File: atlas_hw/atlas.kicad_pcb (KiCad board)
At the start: 4 copper layers, 35.4 x 73.4 mm, 121 parts, among them J1 USB_B_Micro, J10 PSP_LCD, J2 DEBUG_STM, J3 PSP_TOUCH, J4 Conn_02x10_Counter_Clockwise, J8 Micro_SD_Card_Det, J9 PSP_LCD_BL, Q4 Q_NMOS_DGS, SW1 SReset, SW2 Power, SW3 ResetSTM, U1 STM32H723VITx, U11 STM6601CA2BDM6F, U12 BGU7007, U13 LSF0108, U14 NPP600SNADJ, U16 PAM2841, U2 W957A8MFYA5I, U3 MCP1811B, U4 TLV62569DBV, U7 Teseo-LIV3F, Y1 16M, Y4 32k

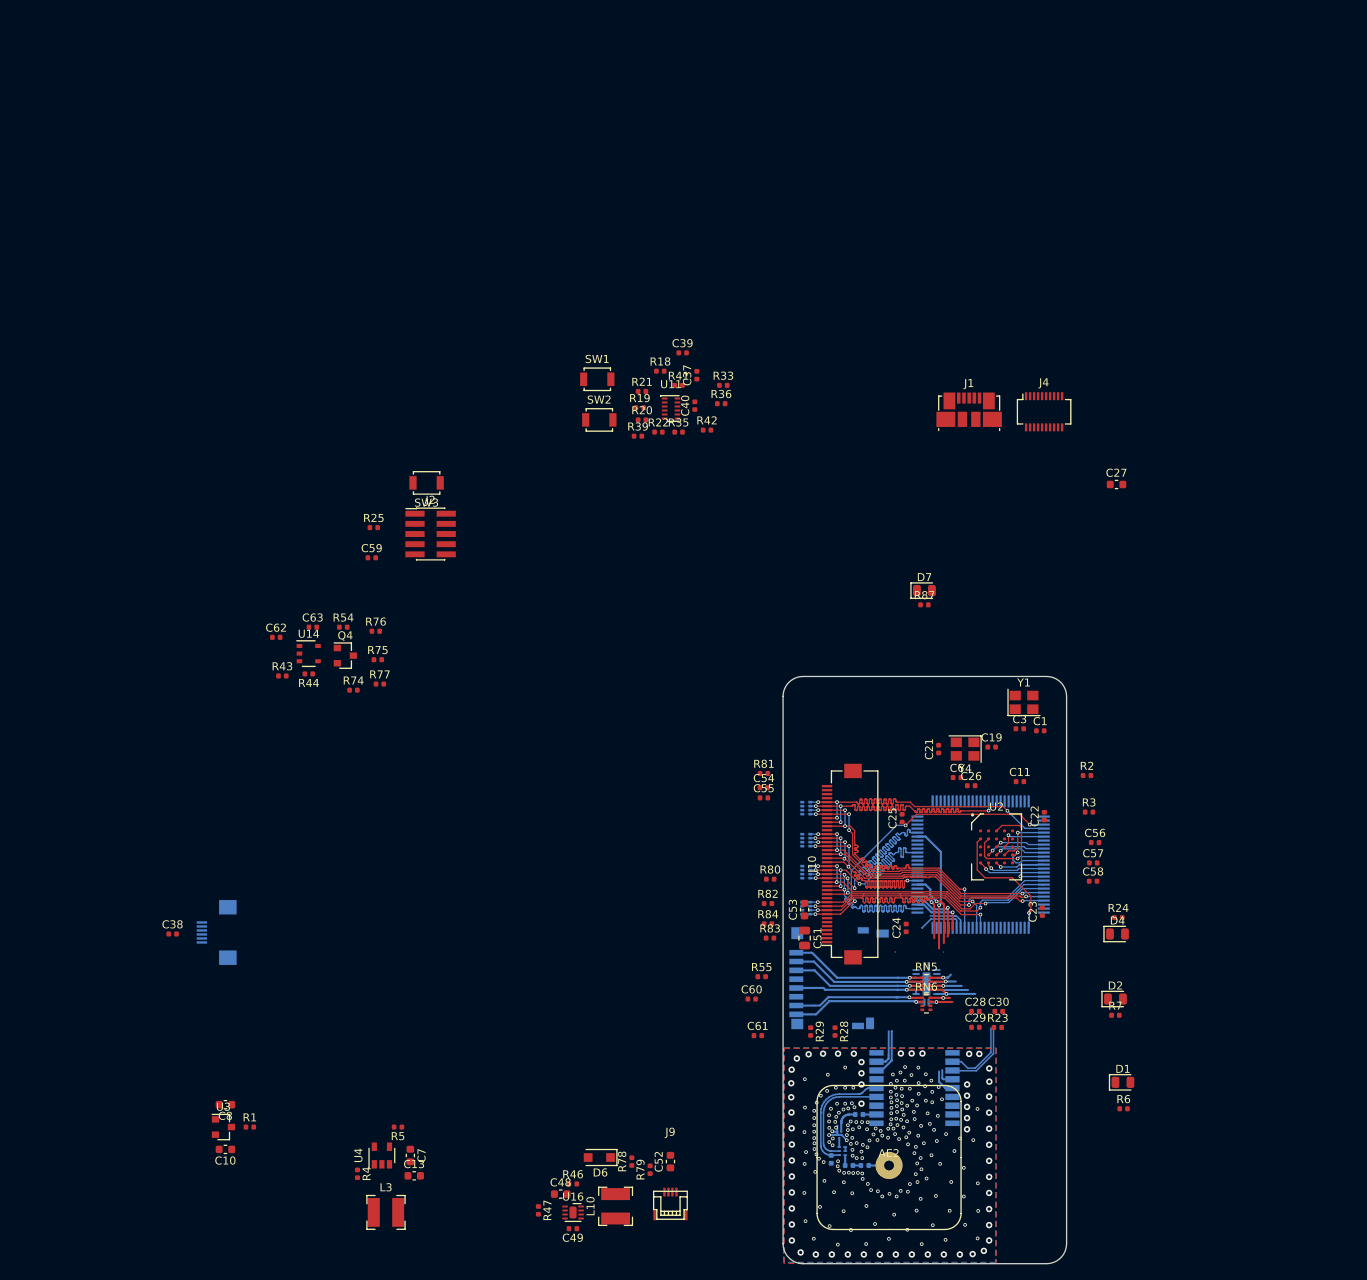
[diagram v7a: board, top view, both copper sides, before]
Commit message: more lite layout
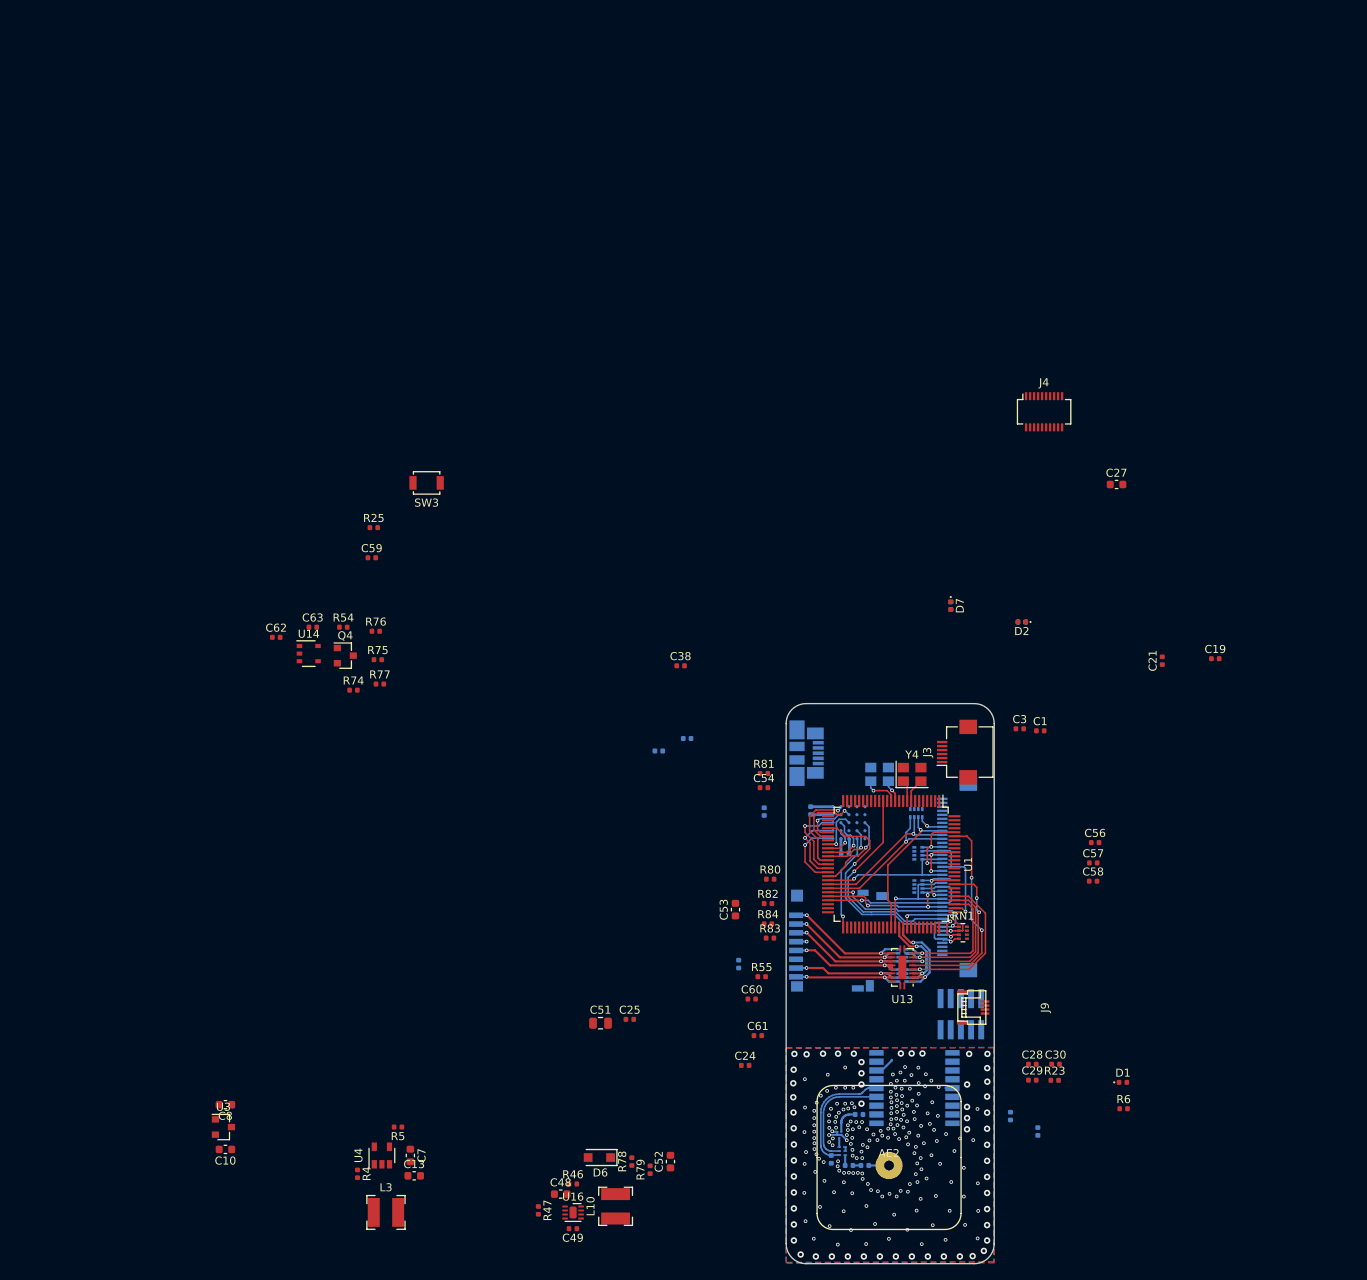
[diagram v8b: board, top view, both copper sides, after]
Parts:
- removed C37, C40: 10u, Capacitor_SMD:C_0402_1005Metric
- removed C39: 0.1u, Capacitor_SMD:C_0402_1005Metric
- removed D4: MCU_ON, LED_SMD:LED_0805_2012Metric
- removed R1, R19, R2, R3, R43, R44: 0, Resistor_SMD:R_0402_1005Metric
- removed R18, R20, R21, R22, R41, R42: NP, Resistor_SMD:R_0402_1005Metric
- removed R24, R35: 1k, Resistor_SMD:R_0402_1005Metric
- removed R33, R36, R39: 100k, Resistor_SMD:R_0402_1005Metric
- removed SW1: SReset, Button_Switch_SMD:SW_SPST_B3U-1000P
- removed SW2: Power, Button_Switch_SMD:SW_SPST_B3U-1000P
- removed U11: STM6601CA2BDM6F, Package_DFN_QFN:TDFN-12_2x3mm_P0.5mm
- C11, C22, C23, C26, C55, C6, J1, J10, J2, R28, R29, R7, R87, RN5, RN6, U2, Y1: moved to B.Cu
- D1, D2, D7: footprint LED_SMD:LED_0805_2012Metric -> LED_SMD:LED_0402_1005Metric
- J3, RN1, U1, U13: moved to F.Cu
- moved J3 95.2 mm to (215.1, 116.5), turned to 90 degrees
- moved J2 89.4 mm to (215.6, 149.2), turned to 90 degrees
- moved C38 71.8 mm to (180.6, 105.7)
- moved R7 50.5 mm to (223.2, 100.2), turned to 180 degrees
- moved D2 48.6 mm to (223.2, 100.2), turned to 180 degrees
- moved J1 47.5 mm to (196.3, 116.6), turned to 90 degrees
- moved J9 45.6 mm to (218.7, 148.4), turned to 270 degrees
- moved C11 45.3 mm to (177.9, 116.3), turned to 180 degrees
- moved C25 42.3 mm to (174.2, 149.9), turned to 0 degrees
- moved C23 38.5 mm to (187.8, 142.9)
- moved C6 34.1 mm to (181.4, 114.8)
- moved C19 30.1 mm to (247.4, 104.8)
- moved C21 30.1 mm to (240.8, 105.0)
- moved R28 28.3 mm to (225.2, 163.9)
- moved C51 27.6 mm to (170.6, 150.3), turned to 0 degrees
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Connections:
- C11 pad 1: Net-(C11-Pad1) -> /VCC_MCU_3V3
- C6 pad 1: Net-(C6-Pad1) -> /VCC_BACKUP
- C62 pad 1: Net-(C62-Pad1) -> /VCC_MCU_3V3
- RN1 pad 1: /LTDC_R4 -> /LTDC_R7
- RN1 pad 2: /LTDC_R5 -> /LTDC_R6
- RN1 pad 3: /LTDC_R6 -> /LTDC_R5
- RN1 pad 4: /LTDC_R7 -> /LTDC_R4
- RN2 pad 1: /LTDC_G4 -> /LTDC_G7
- RN2 pad 2: /LTDC_G5 -> /LTDC_G6
- RN2 pad 3: /LTDC_G6 -> /LTDC_G5
- RN2 pad 4: /LTDC_G7 -> /LTDC_G4
- RN3 pad 1: /LTDC_B4 -> /LTDC_B7
- RN3 pad 2: /LTDC_B5 -> /LTDC_B6
- RN3 pad 3: /LTDC_B6 -> /LTDC_B5
- RN3 pad 4: /LTDC_B7 -> /LTDC_B4
- RN4 pad 1: /LTDC_CK -> /LTDC_VS
- RN4 pad 2: /LTDC_DE -> /LTDC_HS
- RN4 pad 3: /LTDC_HS -> /LTDC_DE
- RN4 pad 4: /LTDC_VS -> /LTDC_CK
- RN5 pad 1: /SD_D2 -> /SDMMC1_D2
- RN5 pad 2: /SD_D3 -> /SDMMC1_D3
- RN5 pad 3: /SD_CMD -> GND
- RN5 pad 4: /SD_CLK -> /SDMMC1_CMD
- RN5 pad 5: /SDMMC1_CK -> /SD_CMD
- RN5 pad 6: /SDMMC1_CMD -> GND
- RN5 pad 7: /SDMMC1_D3 -> /SD_D3
- RN5 pad 8: /SDMMC1_D2 -> /SD_D2
- RN6 pad 1: /SD_D0 -> /SDMMC1_CK
- RN6 pad 2: /SD_D1 -> GND
- RN6 pad 3: GND -> /SDMMC1_D0
- RN6 pad 4: GND -> /SDMMC1_D1
- RN6 pad 5: GND -> /SD_D1
- RN6 pad 6: GND -> /SD_D0
- RN6 pad 7: /SDMMC1_D1 -> GND
- RN6 pad 8: /SDMMC1_D0 -> /SD_CLK
- U1 pad 19: Net-(R2-Pad1) -> GND
- U1 pad 21: Net-(C11-Pad1) -> /VCC_MCU_3V3
- U1 pad 6: Net-(C6-Pad1) -> /VCC_BACKUP
- U13 pad 10: /SDMMC1_D1 -> GND
- U13 pad 11: /SD_D1 -> GND
- U13 pad 12: /SD_D0 -> /SD_D2
- U13 pad 13: /SD_CLK -> /SD_D3
- U13 pad 14: /SD_CLK -> /SD_CMD
- U13 pad 15: /SD_CMD -> /SD_CLK
- U13 pad 16: /SD_D3 -> /SD_CLK
- U13 pad 17: /SD_D2 -> /SD_D0
- U13 pad 18: GND -> /SD_D1
- U13 pad 3: GND -> /SDMMC1_D1
- U13 pad 4: /SDMMC1_D2 -> /SDMMC1_D0
- U13 pad 5: /SDMMC1_D3 -> /SDMMC1_CK
- U13 pad 6: /SDMMC1_CMD -> /SDMMC1_CKIN
- U13 pad 7: /SDMMC1_CKIN -> /SDMMC1_CMD
- U13 pad 8: /SDMMC1_CK -> /SDMMC1_D3
- U13 pad 9: /SDMMC1_D0 -> /SDMMC1_D2
- U14 pad 1: Net-(C62-Pad1) -> /VCC_MCU_3V3
- U14 pad 3: Net-(R43-Pad2) -> /VCC_MCU_3V3
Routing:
- net /LTDC_VS: track 37.8 -> 3.58 mm, vias 4 -> 1
- net /LTDC_G7: track 37.1 -> 9.43 mm, vias 4 -> 2
- net /LTDC_B7: track 38.7 -> 11.4 mm, vias 4 -> 2
- net /LTDC_B5: track 35.6 -> 8.99 mm, vias 4 -> 2
- net /LTDC_R6: track 39.4 -> 13.6 mm, vias 4 -> 3
- net /LTDC_B6: track 33.5 -> 15.5 mm, vias 3 -> 1
- net /LTDC_HS: track 36.2 -> 18.6 mm, vias 2 -> 1
- net /LTDC_G6: track 31.0 -> 14.4 mm, vias 4 -> 1
- net /LTDC_B4: track 35.3 -> 19.0 mm, vias 4 -> 1
- net /LTDC_G4: track 35.1 -> 19.6 mm, vias 4 -> 3
- net /LTDC_R7: track 36.2 -> 21.2 mm, vias 4 -> 2
- net /LPUART1_RX_GPS: track 15.5 -> 0.72 mm
- net /LTDC_G5: track 35.6 -> 21.0 mm, vias 4 -> 1
- net /LPUART1_TX_GPS: track 14.0 -> 0.00 mm
- net /LTDC_DE: track 32.4 -> 19.1 mm, vias 2 -> 1
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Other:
- board size 35.4 x 73.4 mm -> 26 x 70 mm
